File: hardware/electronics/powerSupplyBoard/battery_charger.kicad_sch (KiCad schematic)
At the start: 37 parts, among them J5 Barrel_Jack_Switch, J6 S2B-PH-SM4-TB, J7 PREC002SAAN-RC, J8 PREC003SAAN-RC, Q1 BUK961R6, U4 BQ25798

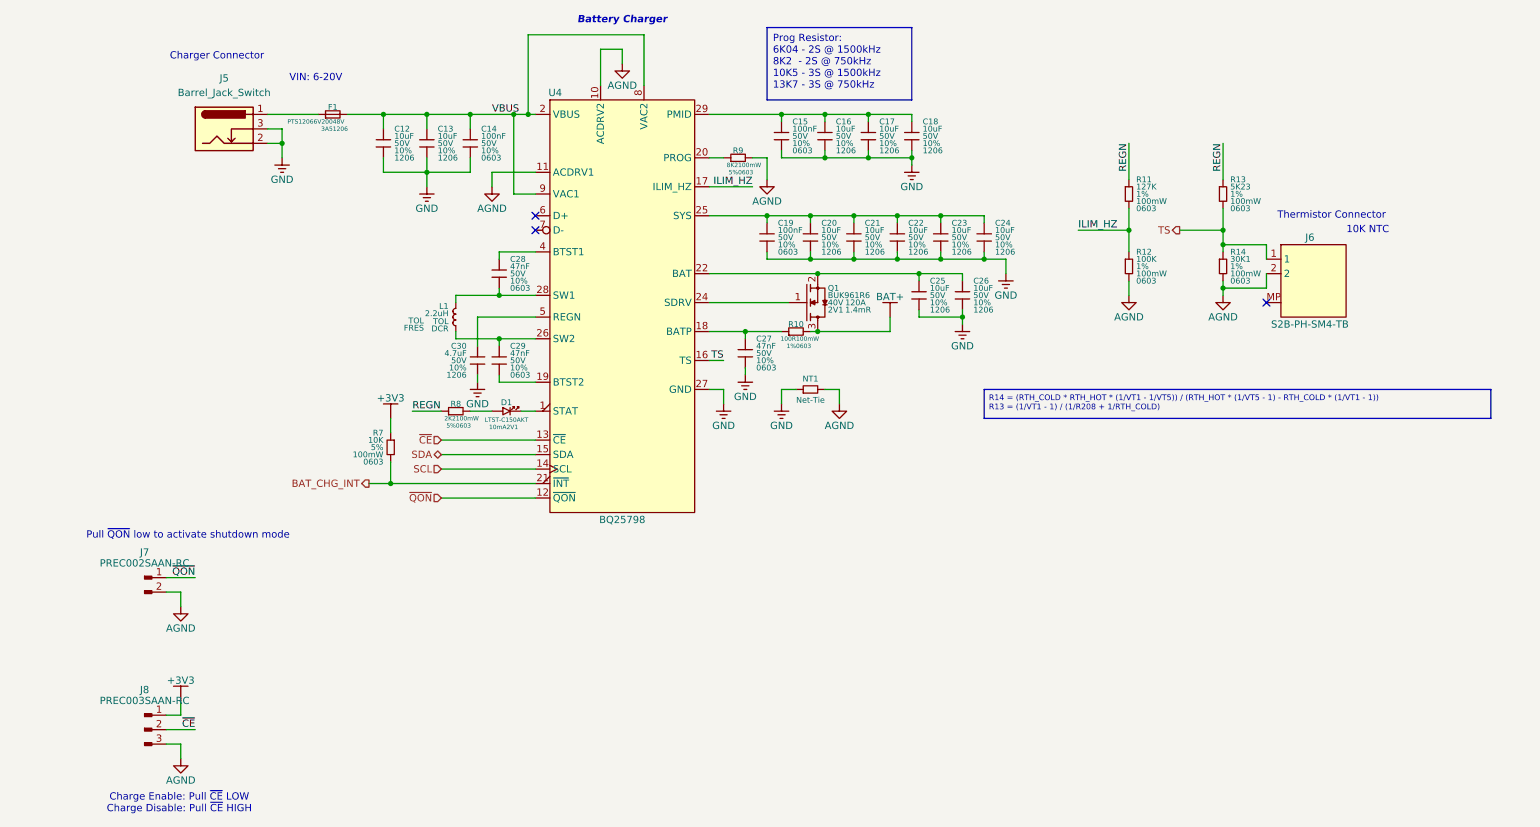
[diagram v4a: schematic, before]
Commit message: fixed component properties and added calculations for resistor dividers
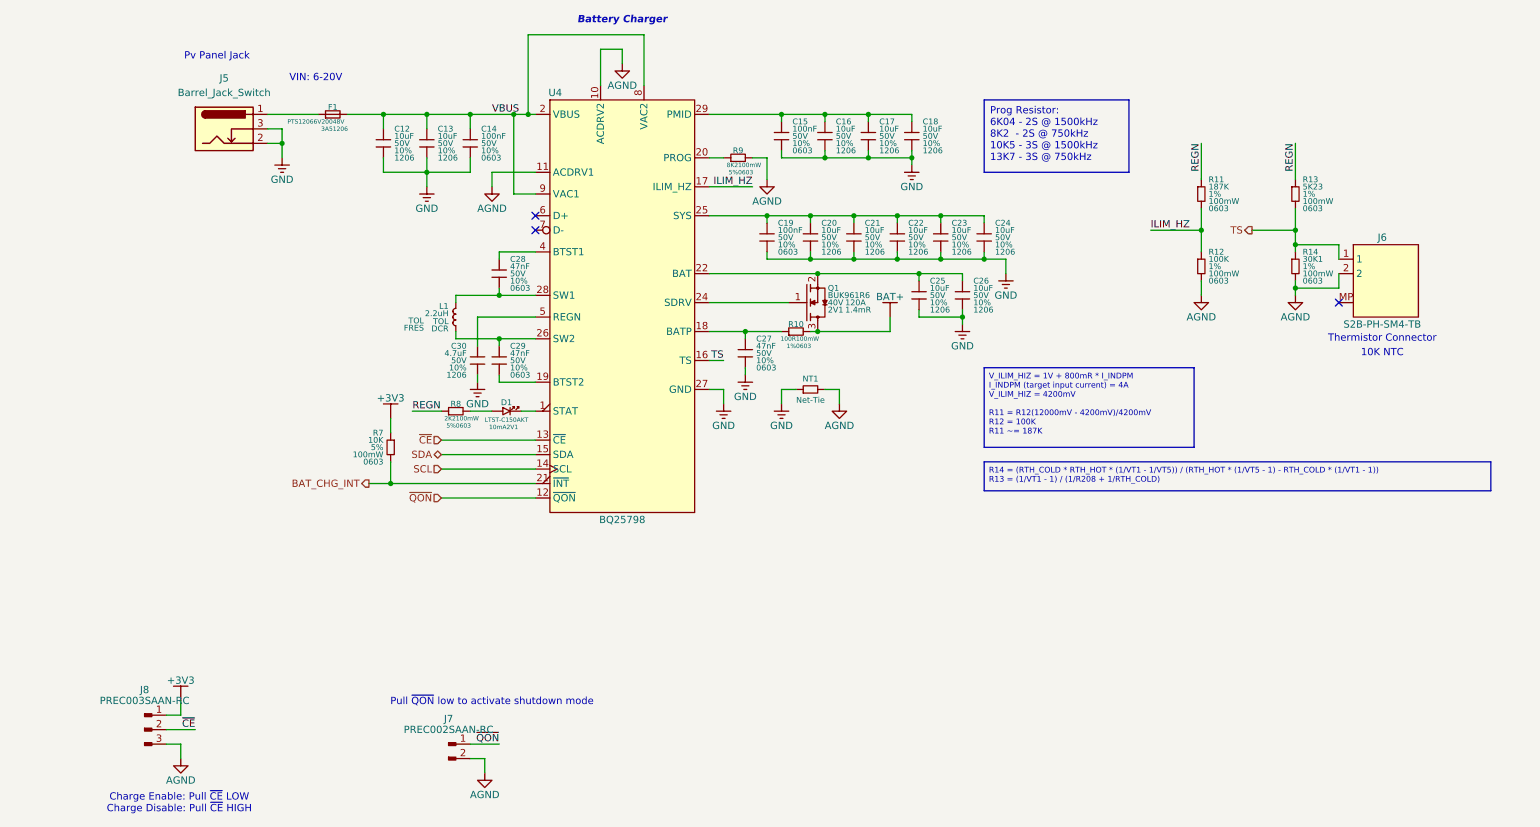
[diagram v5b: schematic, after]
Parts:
- R11: value 127K -> 187K; DKPN 541-127KHCT-ND -> 541-187KHCT-ND; MPN CRCW0603127KFKEA -> CRCW0603187KFKEA
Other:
- note added: "Pv Panel Jack"
- note removed: "Charger Connector"
- moved on the sheet: J6, J7, R11, R12, R13, R14

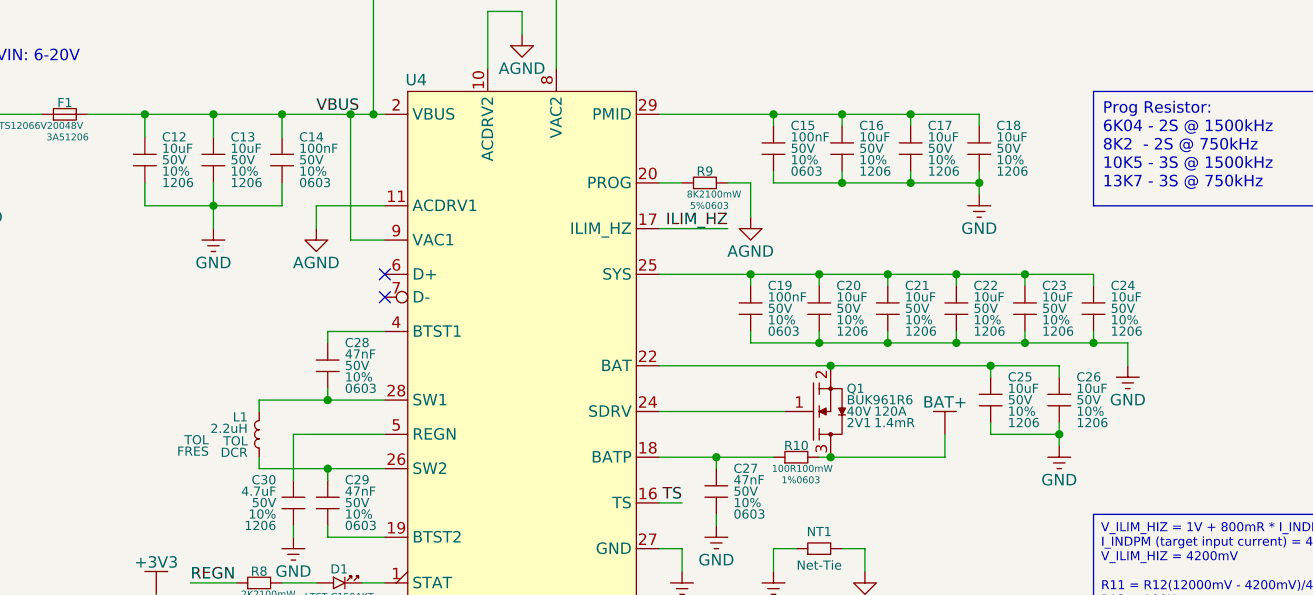
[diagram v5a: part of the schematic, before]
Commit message: redefined footprint paths
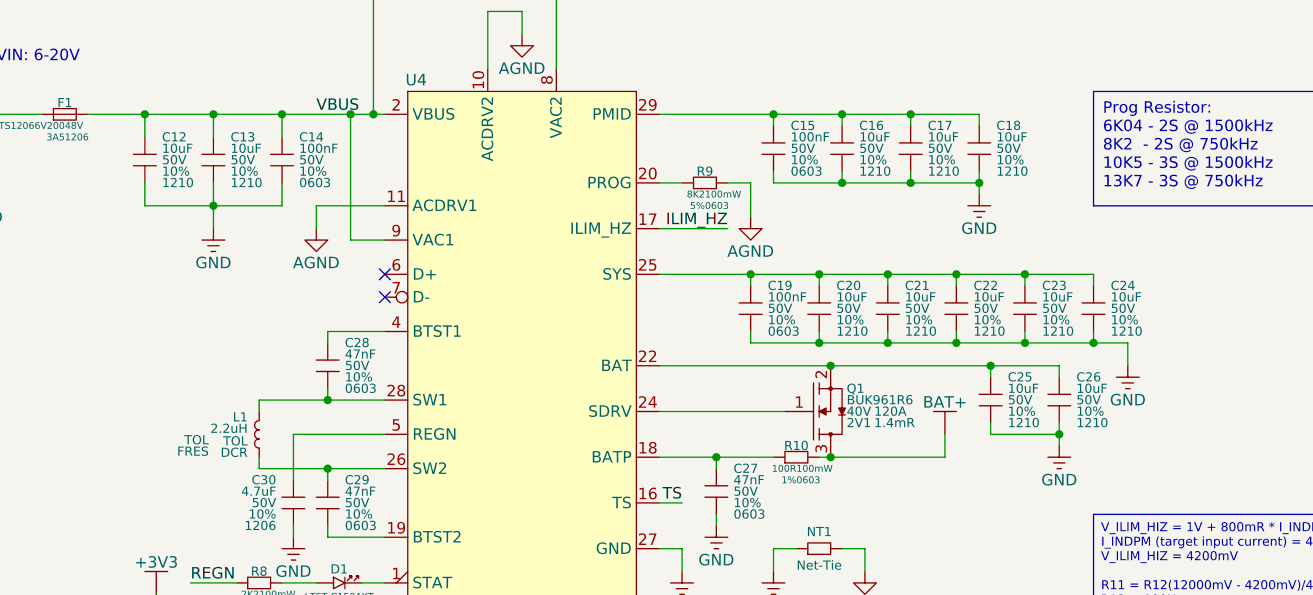
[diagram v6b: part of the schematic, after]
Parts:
- C12, C13, C16, C17, C18, C20, C21, C22, C23, C24, C25, C26: footprint DS-Capacitors-SMD:MLCC1206 -> lib_fp:MLCC1210; MPN 12105C106K4T2A -> KAM32LR71H106KU; Package 1206 -> 1210
- C14, C15, C19: footprint DS-Capacitors-SMD:MLCC0603 -> lib_fp:MLCC0603; MPN 06035C104K4T4A -> KAM15AR71H104KM
- C27, C28, C29: footprint DS-Capacitors-SMD:MLCC0603 -> lib_fp:MLCC0603
- C30: footprint DS-Capacitors-SMD:MLCC1206 -> lib_fp:MLCC1206
- D1: footprint DS-LED-SMD:LTST-1206 -> lib_fp:LTST-1206
- F1: footprint DS-Fuses:PTS1206 -> lib_fp:PTS1206
- J5: footprint DS-Battery-Connectors:PJ-002A -> lib_fp:PJ-002A
- J6: footprint DS-Rectangular-Connectors:JST-PH-S2B-SM4-TB -> lib_fp:JST-PH-S2B-SM4-TB
- J7: footprint DS-Rectangular-Connectors:conn_01x02_254 -> lib_fp:conn_01x02_254
- J8: footprint DS-Rectangular-Connectors:conn_01x03_254 -> lib_fp:conn_01x03_254
- L1: footprint DS-Inductors-SMD:HCM1A1105V2 -> lib_fp:HCM1A1105V2
- NT1: footprint DS-Resistors-SMD:CRCW1210 -> lib_fp:CRCW2010
- Q1: footprint DS-Package-SO:SOT404 -> lib_fp:SOT404
- R10, R11, R12, R13, R14, R7, R8, R9: footprint DS-Resistors-SMD:CRCW0603 -> lib_fp:CRCW0603
- U4: footprint DS-PMIC-SMD:RQM0029A -> lib_fp:RQM0029A
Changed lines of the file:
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@@
 			)
 		)
-		(property "Footprint" "DS-Rectangular-Connectors:conn_01x02_254"
+		(property "Footprint" "lib_fp:conn_01x02_254"
 			(at 85.09 191.77 0)
 			(effects
@@
 			)
 		)
-		(property "Footprint" "DS-Capacitors-SMD:MLCC0603"
+		(property "Footprint" "lib_fp:MLCC0603"
 			(at 142.24 80.645 0)
 			(effects
@@
 			)
 		)
-		(property "MPN" "06035C104K4T4A"
+		(property "MPN" "KAM15AR71H104KM"
 			(at 142.24 80.645 0)
 			(effects
@@
 			)
 		)
-		(property "Footprint" "DS-Capacitors-SMD:MLCC0603"
+		(property "Footprint" "lib_fp:MLCC0603"
 			(at 87.63 81.915 0)
 			(effects
@@
 			)
 		)
-		(property "MPN" "06035C104K4T4A"
+		(property "MPN" "KAM15AR71H104KM"
 			(at 87.63 81.915 0)
 			(effects
@@
 			)
 		)
-		(property "Footprint" "DS-Fuses:PTS1206"
+		(property "Footprint" "lib_fp:PTS1206"
 			(at 63.5 78.74 90)
 			(effects
@@
 			)
 		)
-		(property "Footprint" "DS-Capacitors-SMD:MLCC1206"
+		(property "Footprint" "lib_fp:MLCC1210"
 			(at 173.99 108.585 0)
 			(effects
@@
 			)
 		)
-		(property "MPN" "12105C106K4T2A"
+		(property "MPN" "KAM32LR71H106KU"
 			(at 173.99 108.585 0)
 			(effects
@@
 			)
 		)
-		(property "Package" "1206"
+		(property "Package" "1210"
 			(at 175.895 113.03 0)
 			(do_not_autoplace yes)
@@
 			)
 		)
-		(property "Footprint" "DS-Capacitors-SMD:MLCC0603"
+		(property "Footprint" "lib_fp:MLCC0603"
 			(at 92.71 104.775 0)
 			(effects
@@
 			)
 		)
-		(property "Footprint" "DS-Capacitors-SMD:MLCC1206"
+		(property "Footprint" "lib_fp:MLCC1210"
 			(at 162.56 98.425 0)
 			(effects
@@
 			)
 		)
-		(property "MPN" "12105C106K4T2A"
+		(property "MPN" "KAM32LR71H106KU"
 			(at 162.56 98.425 0)
 			(effects
@@
 			)
 		)
-		(property "Package" "1206"
+		(property "Package" "1210"
 			(at 164.465 102.87 0)
 			(do_not_autoplace yes)
@@
 			)
 		)
-		(property "Footprint" "DS-Resistors-SMD:CRCW0603"
+		(property "Footprint" "lib_fp:CRCW0603"
 			(at 232.41 102.87 0)
 			(effects
@@
 			)
 		)
-		(property "Footprint" "DS-Capacitors-SMD:MLCC1206"
+		(property "Footprint" "lib_fp:MLCC1210"
 			(at 80.01 81.915 0)
 			(effects
@@
 			)
 		)
-		(property "MPN" "12105C106K4T2A"
+		(property "MPN" "KAM32LR71H106KU"
 			(at 80.01 81.915 0)
 			(effects
@@
 			)
 		)
-		(property "Package" "1206"
+		(property "Package" "1210"
 			(at 81.915 86.36 0)
 			(do_not_autoplace yes)
@@
 			)
 		)
-		(property "Footprint" "DS-Resistors-SMD:CRCW0603"
+		(property "Footprint" "lib_fp:CRCW0603"
 			(at 73.66 134.62 0)
 			(effects
@@
 			)
 		)
-		(property "Footprint" "DS-Rectangular-Connectors:conn_01x03_254"
+		(property "Footprint" "lib_fp:conn_01x03_254"
 			(at 31.75 186.69 0)
 			(effects
@@
 			)
 		)
-		(property "Footprint" "DS-Capacitors-SMD:MLCC0603"
+		(property "Footprint" "lib_fp:MLCC0603"
 			(at 139.7 98.425 0)
 			(effects
@@
 			)
 		)
-		(property "MPN" "06035C104K4T4A"
+		(property "MPN" "KAM15AR71H104KM"
 			(at 139.7 98.425 0)
 			(effects
@@
 			)
 		)
-		(property "Footprint" "DS-Capacitors-SMD:MLCC1206"
+		(property "Footprint" "lib_fp:MLCC1210"
 			(at 165.1 80.645 0)
 			(effects
@@
 			)
 		)
-		(property "MPN" "12105C106K4T2A"
+		(property "MPN" "KAM32LR71H106KU"
 			(at 165.1 80.645 0)
 			(effects
@@
 			)
 		)
-		(property "Package" "1206"
+		(property "Package" "1210"
 			(at 167.005 85.09 0)
 			(do_not_autoplace yes)
@@
 			)
 		)
-		(property "Footprint" "DS-PMIC-SMD:RQM0029A"
+		(property "Footprint" "lib_fp:RQM0029A"
 			(at 114.3 110.49 0)
 			(effects
@@
 			)
 		)
-		(property "Footprint" "DS-Resistors-SMD:CRCW0603"
+		(property "Footprint" "lib_fp:CRCW0603"
 			(at 215.9 102.87 0)
 			(effects
@@
 			)
 		)
-		(property "Footprint" "DS-Capacitors-SMD:MLCC1206"
+		(property "Footprint" "lib_fp:MLCC1210"
 			(at 177.8 98.425 0)
 			(effects
@@
 			)
 		)
-		(property "MPN" "12105C106K4T2A"
+		(property "MPN" "KAM32LR71H106KU"
 			(at 177.8 98.425 0)
 			(effects
@@
 			)
 		)
-		(property "Package" "1206"
+		(property "Package" "1210"
 			(at 179.705 102.87 0)
 			(do_not_autoplace yes)
@@
 			)
 		)
-		(property "Footprint" "DS-Resistors-SMD:CRCW1210"
+		(property "Footprint" "lib_fp:CRCW2010"
 			(at 144.78 127 0)
 			(effects
@@
 			)
 		)
-		(property "Footprint" "DS-Battery-Connectors:PJ-002A"
+		(property "Footprint" "lib_fp:PJ-002A"
 			(at 45.72 82.296 0)
 			(effects
@@
 			)
 		)
-		(property "Footprint" "DS-Resistors-SMD:CRCW0603"
+		(property "Footprint" "lib_fp:CRCW0603"
 			(at 142.24 116.84 90)
 			(effects
@@
 			)
 		)
-		(property "Footprint" "DS-Capacitors-SMD:MLCC1206"
+		(property "Footprint" "lib_fp:MLCC1210"
 			(at 149.86 80.645 0)
 			(effects
@@
 			)
 		)
-		(property "MPN" "12105C106K4T2A"
+		(property "MPN" "KAM32LR71H106KU"
 			(at 149.86 80.645 0)
 			(effects
@@
 			)
 		)
-		(property "Package" "1206"
+		(property "Package" "1210"
 			(at 151.765 85.09 0)
 			(do_not_autoplace yes)
@@
 			)
 		)
-		(property "Footprint" "DS-Package-SO:SOT404"
+		(property "Footprint" "lib_fp:SOT404"
 			(at 151.13 109.855 90)
 			(effects
@@
 			)
 		)
-		(property "Footprint" "DS-Resistors-SMD:CRCW0603"
+		(property "Footprint" "lib_fp:CRCW0603"
 			(at 132.08 86.36 90)
 			(effects
@@
 			)
 		)
-		(property "Footprint" "DS-Capacitors-SMD:MLCC0603"
+		(property "Footprint" "lib_fp:MLCC0603"
 			(at 135.89 118.745 0)
 			(effects
@@
 			)
 		)
-		(property "Footprint" "DS-Capacitors-SMD:MLCC1206"
+		(property "Footprint" "lib_fp:MLCC1210"
 			(at 157.48 80.645 0)
 			(effects
@@
 			)
 		)
-		(property "MPN" "12105C106K4T2A"
+		(property "MPN" "KAM32LR71H106KU"
 			(at 157.48 80.645 0)
 			(effects
@@
 			)
 		)
-		(property "Package" "1206"
+		(property "Package" "1210"
 			(at 159.385 85.09 0)
 			(do_not_autoplace yes)
@@
 			)
 		)
-		(property "Footprint" "DS-Capacitors-SMD:MLCC1206"
+		(property "Footprint" "lib_fp:MLCC1210"
 			(at 147.32 98.425 0)
 			(effects
@@
 			)
 		)
-		(property "MPN" "12105C106K4T2A"
+		(property "MPN" "KAM32LR71H106KU"
 			(at 147.32 98.425 0)
 			(effects
@@
 			)
 		)
-		(property "Package" "1206"
+		(property "Package" "1210"
 			(at 149.225 102.87 0)
 			(do_not_autoplace yes)
@@
 			)
 		)
-		(property "Footprint" "DS-Capacitors-SMD:MLCC0603"
+		(property "Footprint" "lib_fp:MLCC0603"
 			(at 92.71 120.015 0)
 			(effects
@@
 			)
 		)
-		(property "Footprint" "DS-Inductors-SMD:HCM1A1105V2"
+		(property "Footprint" "lib_fp:HCM1A1105V2"
 			(at 85.09 113.03 90)
 			(effects
@@
 			)
 		)
-		(property "Footprint" "DS-Capacitors-SMD:MLCC1206"
+		(property "Footprint" "lib_fp:MLCC1210"
 			(at 154.94 98.425 0)
 			(effects
@@
 			)
 		)
-		(property "MPN" "12105C106K4T2A"
+		(property "MPN" "KAM32LR71H106KU"
 			(at 154.94 98.425 0)
 			(effects
@@
 			)
 		)
-		(property "Package" "1206"
+		(property "Package" "1210"
 			(at 156.845 102.87 0)
 			(do_not_autoplace yes)
@@
 			)
 		)
-		(property "Footprint" "DS-Capacitors-SMD:MLCC1206"
+		(property "Footprint" "lib_fp:MLCC1210"
 			(at 166.37 108.585 0)
 			(effects
@@
 			)
 		)
-		(property "MPN" "12105C106K4T2A"
+		(property "MPN" "KAM32LR71H106KU"
 			(at 166.37 108.585 0)
 			(effects
@@
 			)
 		)
-		(property "Package" "1206"
+		(property "Package" "1210"
 			(at 168.275 113.03 0)
 			(do_not_autoplace yes)
@@
 			)
 		)
-		(property "Footprint" "DS-Resistors-SMD:CRCW0603"
+		(property "Footprint" "lib_fp:CRCW0603"
 			(at 82.55 130.81 90)
 			(effects
@@
 			)
 		)
-		(property "Footprint" "DS-Resistors-SMD:CRCW0603"
+		(property "Footprint" "lib_fp:CRCW0603"
 			(at 215.9 90.17 0)
 			(effects
@@
 			)
 		)
-		(property "Footprint" "DS-Capacitors-SMD:MLCC1206"
+		(property "Footprint" "lib_fp:MLCC1206"
 			(at 88.9 120.015 0)
 			(effects
@@
 			)
 		)
-		(property "Footprint" "DS-Capacitors-SMD:MLCC1206"
+		(property "Footprint" "lib_fp:MLCC1210"
 			(at 72.39 81.915 0)
 			(effects
@@
 			)
 		)
-		(property "MPN" "12105C106K4T2A"
+		(property "MPN" "KAM32LR71H106KU"
 			(at 72.39 81.915 0)
 			(effects
@@
 			)
 		)
-		(property "Package" "1206"
+		(property "Package" "1210"
 			(at 74.295 86.36 0)
 			(do_not_autoplace yes)
@@
 			)
 		)
-		(property "Footprint" "DS-Resistors-SMD:CRCW0603"
+		(property "Footprint" "lib_fp:CRCW0603"
 			(at 232.41 90.17 0)
 			(effects
@@
 			)
 		)
-		(property "Footprint" "DS-Capacitors-SMD:MLCC1206"
+		(property "Footprint" "lib_fp:MLCC1210"
 			(at 170.18 98.425 0)
 			(effects
@@
 			)
 		)
-		(property "MPN" "12105C106K4T2A"
+		(property "MPN" "KAM32LR71H106KU"
 			(at 170.18 98.425 0)
 			(effects
@@
 			)
 		)
-		(property "Package" "1206"
+		(property "Package" "1210"
 			(at 172.085 102.87 0)
 			(do_not_autoplace yes)
@@
 			)
 		)
-		(property "Footprint" "DS-LED-SMD:LTST-1206"
+		(property "Footprint" "lib_fp:LTST-1206"
 			(at 93.98 130.81 0)
 			(effects
@@
 			)
 		)
-		(property "Footprint" "DS-Rectangular-Connectors:JST-PH-S2B-SM4-TB"
+		(property "Footprint" "lib_fp:JST-PH-S2B-SM4-TB"
 			(at 242.57 101.6 0)
 			(effects
